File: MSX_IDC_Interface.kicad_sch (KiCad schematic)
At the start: 25 parts, among them J1 DE1 GPIO, J2 Conn_01x03_Male, J3 Conn_01x03_Male, J4 Conn_01x03_Male, J5 Conn_01x03_Male, J6 Conn_01x03_Male, J7 Conn_01x03_Male, U1 74LVC245A, U2 74LVC245A, U3 74LVC245A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

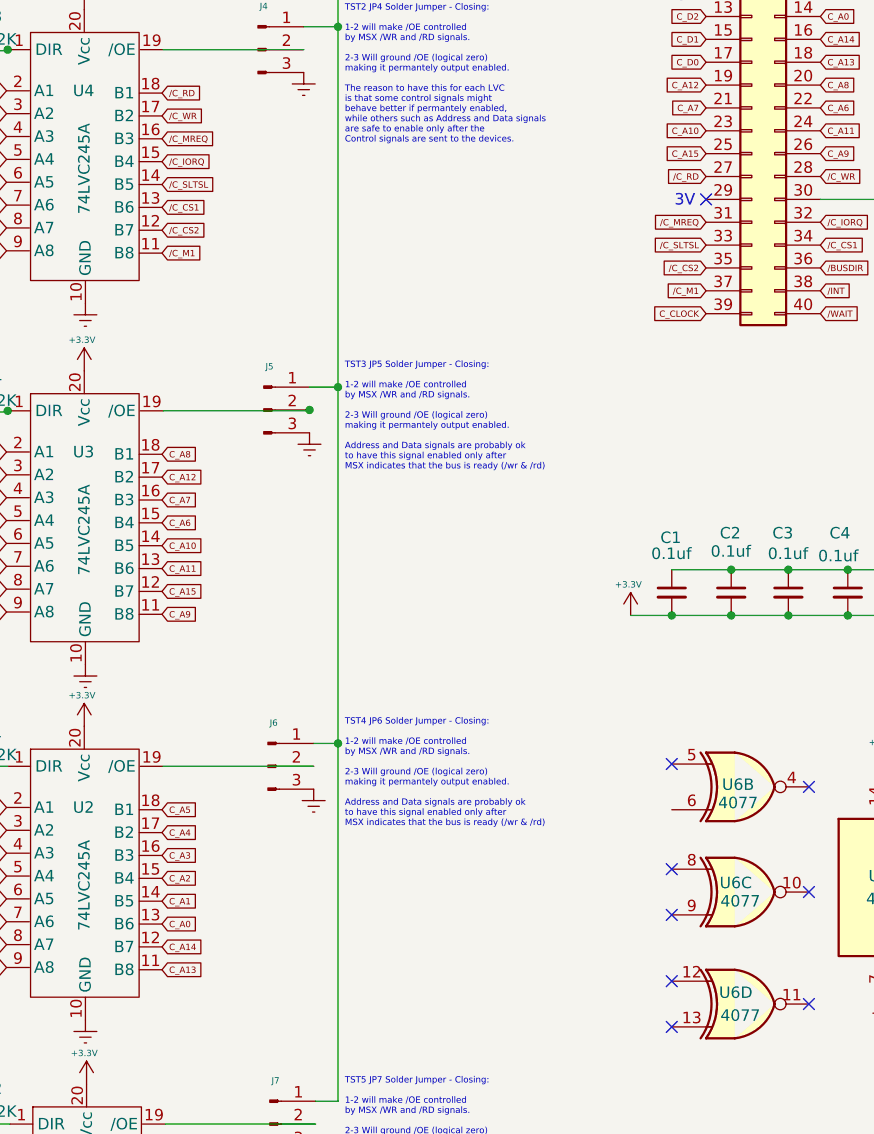
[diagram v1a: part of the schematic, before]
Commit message: Fixed missing 3v input
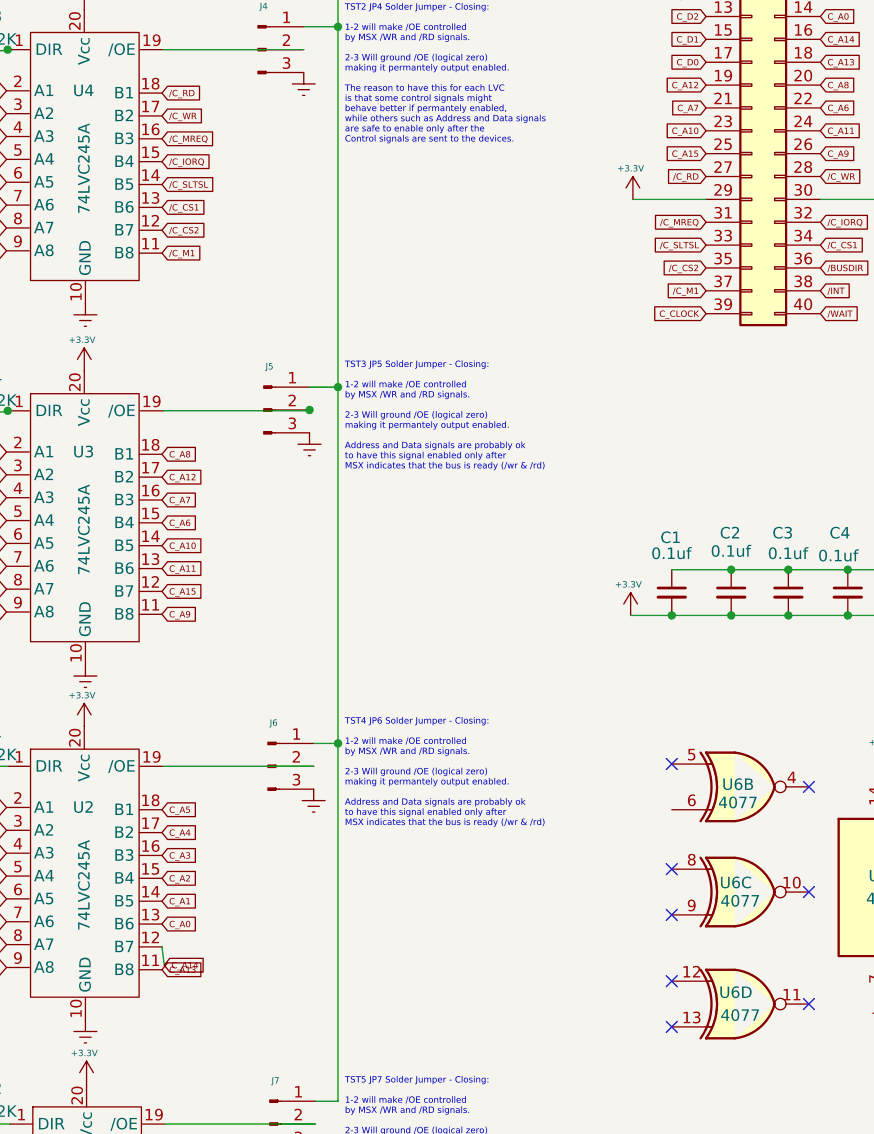
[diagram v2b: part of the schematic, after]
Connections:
- net +3.3V: now also J1.29 (Pin_29)
- no-connect marks 14 -> 13
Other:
- note removed: "3V"
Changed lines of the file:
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@@
   (title_block
     (title "MSX IDC Adapter")
-    (rev "1.0")
+    (date "2022-12-13")
+    (rev "1.1")
     (company "RCC")
     (comment 1 "to 3.3v systems with voltage conversion")
@@
   (no_connect (at 32.385 79.248))
   (no_connect (at 32.385 107.188))
-  (no_connect (at 152.908 114.3))
   (wire (pts (xy 70.116 216.916) (xy 70.104 216.916))
     (stroke (width 0) (type default) (color 0 0 0 0))
@@
     (stroke (width 0) (type default) (color 0 0 0 0))
   )
+  (wire (pts (xy 144.78 114.3) (xy 152.908 114.3))
+    (stroke (width 0) (type default) (color 0 0 0 0))
+  )
   (wire (pts (xy 70.116 217.043) (xy 70.116 216.916))
     (stroke (width 0) (type default) (color 0 0 0 0))
@@
   )
   (wire (pts (xy 32.385 193.548) (xy 48.26 193.548))
+    (stroke (width 0) (type default) (color 0 0 0 0))
+  )
+  (wire (pts (xy 92.71 199.39) (xy 92.456 197.358))
     (stroke (width 0) (type default) (color 0 0 0 0))
   )
@@
   (text "Takes Direction from \n/RD signal in MSX BUS" (at 51.816 220.98 0)
     (effects (font (size 1 1)) (justify left bottom))
-  )
-  (text "3V" (at 149.4017 115.2727 0)
-    (effects (font (size 1.27 1.27)) (justify left bottom))
   )
   (text "TST5 JP7 Solder Jumper - Closing:\n\n1-2 will make /OE controlled\nby MSX /WR and /RD signals.\n\n2-3 Will ground /OE (logical zero)\nmaking it permantely output enabled.\n\nAddress and Data signals are probably ok\nto have this signal enabled only after \nMSX indicates that the bus is ready (/wr & /rd)"
@@
     )
   )
-  (global_label "C_A14" (shape input) (at 92.456 197.358 0) (fields_autoplaced)
-    (effects (font (size 0.7 0.7)) (justify left))
-    (property "Intersheet References" "${INTERSHEET_REFS}" (id 0) (at 96.9527 197.3143 0)
+  (global_label "C_A14" (shape input) (at 92.71 199.39 0) (fields_autoplaced)
+    (effects (font (size 0.7 0.7)) (justify left))
+    (property "Intersheet References" "${INTERSHEET_REFS}" (id 0) (at 97.2067 199.3463 0)
       (effects (font (size 0.7 0.7)) (justify left) hide)
     )
@@
     )
     (property "Datasheet" "" (id 3) (at 108.204 60.706 0)
+      (effects (font (size 1.27 1.27)) hide)
+    )
+    (pin "1")
+  )
+  (symbol (lib_id "power:+3.3V") (at 144.78 114.3 0) (unit 1)
+    (in_bom yes) (on_board yes)
+    (property "Reference" "#PWR0109" (id 0) (at 144.78 118.11 0)
+      (effects (font (size 1.27 1.27)) hide)
+    )
+    (property "Value" "+3.3V" (id 1) (at 144.526 110.871 0)
+      (effects (font (size 0.7 0.7)))
+    )
+    (property "Footprint" "" (id 2) (at 144.78 114.3 0)
+      (effects (font (size 1.27 1.27)) hide)
+    )
+    (property "Datasheet" "" (id 3) (at 144.78 114.3 0)
       (effects (font (size 1.27 1.27)) hide)
     )
@@
       (reference "#PWR0108") (unit 1) (value "GNDREF") (footprint "")
     )
+    (path "/35c824a2-9795-4f88-9ed3-97c330fc9e40"
+      (reference "#PWR0109") (unit 1) (value "+3.3V") (footprint "")
+    )
     (path "/d88b88a1-3a49-411f-ab35-844e3052fd45"
